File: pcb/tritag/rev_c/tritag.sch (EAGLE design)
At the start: 135 parts, among them J1 TC2030-JLINK-NL, J2 TC2030-JLINK-NL, J3 MICRO_USB_B_HIROSE_ZX62-B-5PA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, J5 BAT_HOLE, J7 CON_MICRO_SDDM3AT-SF-PEJM5, T1 HHM1595A1, U1 NRF52840, U12 SIP32510, U2 MCP73831, U3 FT232RQ, U4 MAX8887EZK33+T, U5 STM32F091CC, U6 SKY13317, U7 LXDC2HN18A, U8 DW1000, U9 LIS2DW12, X1 32MHz, X2 38.4M, X3 16M, X4 32.768kHz

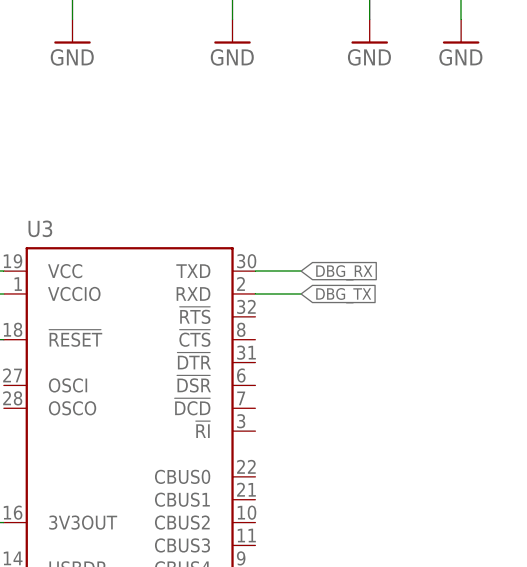
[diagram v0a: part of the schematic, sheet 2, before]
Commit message: added clearance for screws, decoupled FT232 to reduce power draw, added power planes
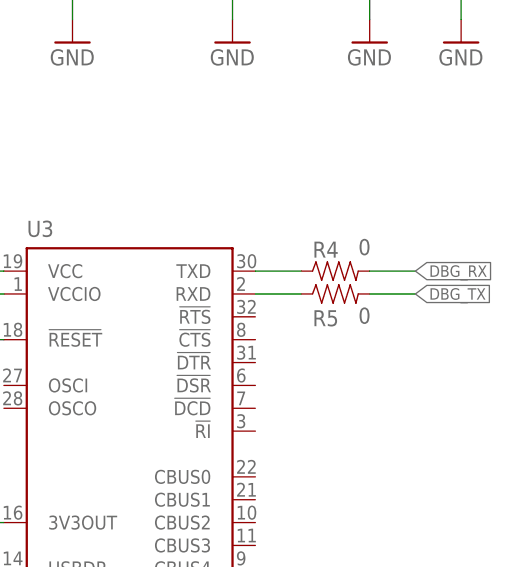
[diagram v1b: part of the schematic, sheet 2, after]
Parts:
- added R4, R5: 0, passives:RESISTOR0402_RES
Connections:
- new net N$33: R4.1, U3.TXD
- new net N$34: R5.1, U3.RXD
- net DBG_RX: now also R4.2; no longer U3.TXD
- net DBG_TX: now also R5.2; no longer U3.RXD
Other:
- note added: "Mount 0-Ohm resistors only if you intend to use the FTDI; this prevents unintentional power draws"
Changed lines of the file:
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@@
 <part name="TP12" library="headers" deviceset="TEST-POINT" device=""/>
 <part name="TP15" library="testpad" library_urn="urn:adsk.eagle:library:385" deviceset="TP" device="TP06SQ" package3d_urn="urn:adsk.eagle:package:27952/1"/>
+<part name="R4" library="passives" deviceset="RESISTOR" device="0402_RES" value="0"/>
+<part name="R5" library="passives" deviceset="RESISTOR" device="0402_RES" value="0"/>
 </parts>
 <sheets>
@@
 <wire x1="147.32" y1="55.88" x2="147.32" y2="53.34" width="0.1524" layer="98" style="longdash"/>
 <wire x1="147.32" y1="53.34" x2="147.32" y2="20.32" width="0.1524" layer="98" style="longdash"/>
-<text x="157.48" y="30.48" size="5.08" layer="98">USB-Serial</text>
+<text x="152.4" y="30.48" size="5.08" layer="98">USB-Serial</text>
 <text x="3.556" y="49.784" size="3.81" layer="98">SD Card Adapter</text>
 <wire x1="0" y1="55.88" x2="93.98" y2="55.88" width="0.1524" layer="98" style="longdash"/>
@@
 <wire x1="93.98" y1="55.88" x2="147.32" y2="55.88" width="0.1524" layer="98" style="longdash"/>
 <wire x1="93.98" y1="116.84" x2="93.98" y2="55.88" width="0.1524" layer="98" style="longdash"/>
+<text x="203.2" y="30.48" size="1.778" layer="98">Mount 0-Ohm resistors only
+if you intend to use the FTDI;
+this prevents unintentional
+power draws</text>
 </plain>
 <instances>
@@
 <instance part="A2" gate="G$1" x="119.38" y="88.9"/>
 <instance part="A1" gate="G$1" x="109.22" y="91.44"/>
+<instance part="R4" gate="G$1" x="231.14" y="101.6" smashed="yes">
+<attribute name="NAME" x="227.33" y="103.0986" size="1.778" layer="95"/>
+<attribute name="VALUE" x="232.41" y="103.378" size="1.778" layer="96"/>
+</instance>
+<instance part="R5" gate="G$1" x="231.14" y="99.06" smashed="yes">
+<attribute name="NAME" x="227.33" y="95.4786" size="1.778" layer="95"/>
+<attribute name="VALUE" x="232.41" y="95.758" size="1.778" layer="96"/>
+</instance>
 </instances>
 <busses>
@@
 <wire x1="58.42" y1="152.4" x2="63.5" y2="152.4" width="0.1524" layer="91"/>
 <label x="63.5" y="152.4" size="1.016" layer="95" xref="yes"/>
-</segment>
-</net>
-<net name="DBG_RX" class="0">
-<segment>
-<label x="226.06" y="101.6" size="1.27" layer="95" xref="yes"/>
-<pinref part="U3" gate="1" pin="TXD"/>
-<wire x1="220.98" y1="101.6" x2="226.06" y2="101.6" width="0.1524" layer="91"/>
 </segment>
 </net>
@@
 </segment>
 </net>
-<net name="DBG_TX" class="0">
-<segment>
-<pinref part="U3" gate="1" pin="RXD"/>
-<wire x1="220.98" y1="99.06" x2="226.06" y2="99.06" width="0.1524" layer="91"/>
-<label x="226.06" y="99.06" size="1.27" layer="95" xref="yes"/>
-</segment>
-</net>
 <net name="!FT_RST" class="0">
 <segment>
@@
 </segment>
 </net>
+<net name="N$33" class="0">
+<segment>
+<pinref part="U3" gate="1" pin="TXD"/>
+<pinref part="R4" gate="G$1" pin="1"/>
+<wire x1="220.98" y1="101.6" x2="226.06" y2="101.6" width="0.1524" layer="91"/>
+</segment>
+</net>
+<net name="N$34" class="0">
+<segment>
+<pinref part="U3" gate="1" pin="RXD"/>
+<pinref part="R5" gate="G$1" pin="1"/>
+<wire x1="220.98" y1="99.06" x2="226.06" y2="99.06" width="0.1524" layer="91"/>
+</segment>
+</net>
+<net name="DBG_RX" class="0">
+<segment>
+<pinref part="R4" gate="G$1" pin="2"/>
+<wire x1="233.68" y1="101.6" x2="238.76" y2="101.6" width="0.1524" layer="91"/>
+<label x="238.76" y="101.6" size="1.27" layer="95" xref="yes"/>
+</segment>
+</net>
+<net name="DBG_TX" class="0">
+<segment>
+<pinref part="R5" gate="G$1" pin="2"/>
+<wire x1="233.68" y1="99.06" x2="238.76" y2="99.06" width="0.1524" layer="91"/>
+<label x="238.76" y="99.06" size="1.27" layer="95" xref="yes"/>
+</segment>
+</net>

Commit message: renumbered parts, added decaps for power supply
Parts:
- removed C75: 0.1uF, passives:CAPACITOR0402_CAP
- removed C77: 4.7uF, passives:CAPACITOR0402_CAP
- removed C78: 1pF, passives:CAPACITOR0402_CAP
- removed C79: 1uF, passives:CAPACITOR0402_CAP
- removed C80: 47nF, passives:CAPACITOR0402_CAP
- removed C81, C82: 12pF, passives:CAPACITOR0402_CAP
- removed D5: SML-LX0404SIUPGUSB, leds:SML-LX0404SIUPGUSB
- removed J7: CON_MICRO_SDDM3AT-SF-PEJM5, connector:CON_MICRO_SDDM3AT-SF-PEJM5
- removed R23: 10k, passives:RESISTOR0402_RES
- removed R27, R28, R29: 470, passives:RESISTOR0402_RES
- removed U12: SIP32510, chips:SIP32510
- added C61, C62, C63, C64, C65, C66, C67, C68: 4.7uF, passives:CAPACITOR0402_CAP
- added C70: 10uF, passives:CAPACITOR0603_CAP
- added D3: SML-LX0404SIUPGUSB, leds:SML-LX0404SIUPGUSB
- added J4: TC2030-JLINK-NL, connector:TC2030-JLINK-NL
- added R15: 11k 1%, passives:RESISTOR0402_RES
- added R16: 11k, passives:RESISTOR0402_RES
- added R17: 16k, passives:RESISTOR0402_RES
- added R18: 100k, passives:RESISTOR0402_RES
- added U10: STM32F091CC, chips:STM32F091CC
- C1: value 4.7uF -> 1pF; DIGIKEY 445-5947-1-ND -> 490-6269-1-ND; MPN C1005X5R0J475K050BC -> GRM1555C1HR80BA01D
- C10, C11: value 4.7uF -> 12pF; DIGIKEY (none) -> 490-6197-1-ND; MPN (none) -> GRM1555C1H120GA01D
- C12: DIGIKEY 490-6197-1-ND -> (none); MPN GRM1555C1H120GA01D -> (none)
- C13: value 1uF -> 12pF
- C14: value 1pF -> 12pF; DIGIKEY 490-6269-1-ND -> (none); MPN GRM1555C1HR80BA01D -> (none)
- C15: value 10nF -> 12pF
- C16: value 12pF -> 18pF; device passives:CAPACITOR0201_CAP -> passives:CAPACITOR0402_CAP
- C17: value 12pF -> 27pF; device passives:CAPACITOR0201_CAP -> passives:CAPACITOR0402_CAP
- C18: value 4.7uF -> 100pF; DIGIKEY (none) -> 490-5922-1-ND; MPN (none) -> GRM1555C1H101JA01D
- C19: value 10uF -> 330pF; device passives:CAPACITOR0603_CAP -> passives:CAPACITOR0402_CAP
- C2: value 0.1uF -> 1pF; DIGIKEY 490-6328-1-ND -> 490-6264-1-ND; MPN GRM155R71C104KA88J -> GRM1555C1HR50WA01D
- C20: value 0.1uF -> 330pF
- C21: value 4.7uF -> 820pF; DIGIKEY (none) -> 445-1264-1-ND; MPN (none) -> C1005X7R1C473K050BC
- C22: value 0.1uF -> 820pF
- C23, C24, C25: value 0.1uF -> 10nF
- C26: value 0.1uF -> 47nF; DIGIKEY (none) -> 445-1264-1-ND; MPN (none) -> C1005X7R1C473K050BC
- C28, C29, C30: DIGIKEY (none) -> 490-6328-1-ND; MPN (none) -> GRM155R71C104KA88J
- C3: value 0.1uF -> 1.2pF; DIGIKEY 490-6328-1-ND -> (none); MPN GRM155R71C104KA88J -> (none)
- C31, C32: value 10pF -> 0.1uF; DIGIKEY (none) -> 490-6328-1-ND; MPN (none) -> GRM155R71C104KA88J
- C33: value 330pF -> 0.1uF; DIGIKEY (none) -> 490-6328-1-ND; MPN (none) -> GRM155R71C104KA88J
- C34: value 330pF -> 0.1uF
- C35: value 0.01uF -> 0.1uF
- C4, C5: value 0.1uF -> 10pF; DIGIKEY 490-6328-1-ND -> (none); MPN GRM155R71C104KA88J -> (none)
- C41: value 820pF -> 0.1uF
- C42: value 27pF -> 0.1uF
- C43: value 1.2pF -> 0.1uF
- C44: value 18pF -> 0.1uF
- C45, C46, C47, C48: value 12pF -> 0.1uF
- C49, C50, C51: value 100nF -> 0.1uF
- C52, C53: value 4.7uF -> 0.1uF
- C54: value 100nF -> 1uF
- C55: DIGIKEY (none) -> 490-7195-1-ND; MPN (none) -> GRM155R70G105KA12D
- C56: value 10nF -> 1uF; DIGIKEY (none) -> 490-7195-1-ND; MPN (none) -> GRM155R70G105KA12D
- C57: value 0.1uF -> 1uF
- C59: value 0.1uF -> 4.7uF; DIGIKEY 490-6328-1-ND -> (none); MPN GRM155R71C104KA88J -> (none)
- C6: value 1uF -> 12pF; device passives:CAPACITOR0402_CAP -> passives:CAPACITOR0201_CAP; DIGIKEY 490-7195-1-ND -> (none); MPN GRM155R70G105KA12D -> (none)
- C60: value 820pF -> 4.7uF; DESCRIPTION (none) -> CAP CER 4.7UF 6.3V X5R 0402; DIGIKEY 445-1264-1-ND -> 445-5947-1-ND; MANUFACTURER (none) -> TDK; MPN C1005X7R1C473K050BC -> C1005X5R0J475K050BC
- C7: value 100pF -> 12pF; device passives:CAPACITOR0402_CAP -> passives:CAPACITOR0201_CAP; DIGIKEY 490-5922-1-ND -> (none); MPN GRM1555C1H101JA01D -> (none)
- C9: value 0.1uF -> 12pF; DIGIKEY (none) -> 490-6197-1-ND; MPN (none) -> GRM1555C1H120GA01D
- J1: value TC2030-JLINK-NL -> BAT_HOLE; device connector:TC2030-JLINK-NL -> connector:BAT_HOLE
- J2: value TC2030-JLINK-NL -> CON_MICRO_SDDM3AT-SF-PEJM5; device connector:TC2030-JLINK-NL -> connector:CON_MICRO_SDDM3AT-SF-PEJM5
- J5: value BAT_HOLE -> TC2030-JLINK-NL; device connector:BAT_HOLE -> connector:TC2030-JLINK-NL
- R1: value 270 -> 0
- R10: value 11k -> 1k
- R11: value 1k -> 2k 1%
- R12, R13: value 1k -> 10k
- R14: value 100k -> 10k
- R2: value 1k -> 0
- R21: value 10k -> 2.2M
- R22: value 10k -> 10M
- R3: value 2k 1% -> 270
- R4, R5: value 0 -> 470
- R6: value 16k -> 470
- R7: value 2.2M -> 1k
- R8: value 10M -> 1k
- R9: value 11k 1% -> 1k
- U1: value NRF52840 -> DW1000; device chips:NRF52840 -> chips:DW1000
- U2: value MCP73831 -> FT232RQ; device chips:MCP73831 -> ftdichip:FT232RQ
- U3: value FT232RQ -> LIS2DW12; device ftdichip:FT232RQ -> chips:LIS2DW12
- U4: value MAX8887EZK33+T -> LXDC2HN18A; device chips:MAX8887EZK33+T -> regulators:LXDC2HN18A
- U5: value STM32F091CC -> MAX8887EZK33+T; device chips:STM32F091CC -> chips:MAX8887EZK33+T
- U6: value SKY13317 -> MCP73831; device switches:SKY13317 -> chips:MCP73831
- U7: value LXDC2HN18A -> NRF52840; device regulators:LXDC2HN18A -> chips:NRF52840
- U8: value DW1000 -> SIP32510; device chips:DW1000 -> chips:SIP32510
- U9: value LIS2DW12 -> SKY13317; device chips:LIS2DW12 -> switches:SKY13317
- X1: value 32MHz -> 32.768kHz; device crystals:7V-32.000MAHV-T -> crystals:ABS05-32.768KHZ-9-T
- X2: value 38.4M -> 16MHz; DESCRIPTION 38.4MHz ±10ppm Crystal 8.5pF 40 Ohms 4-SMD, No Lead -> 16MHz ±10ppm Crystal 8pF 80 Ohms 4-SMD, No Lead; DIGIKEY SER3631CT-ND -> SER3913CT-ND
- X3: value 16M -> 32MHz; device crystals:FA-20H -> crystals:7V-32.000MAHV-T; DESCRIPTION 16MHz ±10ppm Crystal 8pF 80 Ohms 4-SMD, No Lead -> (none); DIGIKEY SER3913CT-ND -> (none)
- X4: value 32.768kHz -> 38.4MHz; device crystals:ABS05-32.768KHZ-9-T -> crystals:FA-20H; DESCRIPTION (none) -> 38.4MHz ±10ppm Crystal 8.5pF 40 Ohms 4-SMD, No Lead; DIGIKEY (none) -> SER3631CT-ND
- renumbered C76 to C69
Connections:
- net !CHRG: now also R7.1; no longer R2.1
- net !DW_RST: now also U1.!RST, U10.PB0; no longer U5.PB0, U8.!RST
- net !DW_SPI_CS: now also U1.!SPICS, U10.PA4; no longer U5.PA4, U8.!SPICS
- net !FT_RST: now also U2.!RESET, U7.P1.08; no longer U1.P1.08, U3.!RESET
- net !NRF_CS_IMU: now also U3.CS, U7.P0.16; no longer U1.P0.16, U9.CS
- net !NRF_CS_SD: now also J2.DATA3-CD/CS_N, R13.1, U7.P0.18; no longer J7.DATA3-CD/CS_N, R22.1, U1.P0.18
- net !SD_DETECT: now also J2.A, R19.1, U7.P1.00; no longer J7.A, R20.1, U1.P1.00
- net !STM_RST: now also J5.!RESET, U10.!RST; no longer J2.!RESET, U5.!RST
- net +1V8: now also C34.1, C37.1, C63.1, C70.1, U1.VDDLDOA, U1.VDDLDOD, U4.VOUT; no longer C19.1, C20.1, C21.1, C24.1, U7.VOUT, U8.VDDLDOA, U8.VDDLDOD
- net +3V3: now also C19.1, C20.1, C24.1, C25.1, C29.1, C30.1, C4.1, C44.1, C45.1, C46.1, C47.1, C48.1, C57.1, C59.1, C61.1, C62.2, C64.1, C65.1, C66.1, D3.VDD, J4.VCC, J5.VCC, U1.VDDAON, U1.VDDBAT, U1.VDDIOA, U1.VDDLNA, U1.VDDPA1, U1.VDDPA2, U10.VBAT, U10.VDD/24, U10.VDD/48, U10.VDDA, U10.VDDIO2, U3.VCC, U3.VDD_IO, U4.VIN, U5.OUT, U7.VDD, U7.VDDH, U8.VSUPP; no longer C1.1, C11.1, C18.2, C2.1, C3.1, C32.1, C34.1, C35.1, C36.1, C37.1, C38.1, C39.1, C40.1, C53.1, C54.1, C56.1, C58.1, C6.1, C75.1, D5.VDD, J1.VCC, J2.VCC, U1.VDD, U1.VDDH, U12.VSUPP, U4.OUT, U5.VBAT, U5.VDD/24, U5.VDD/48, U5.VDDA, U5.VDDIO2, U7.VIN, U8.VDDAON, U8.VDDBAT, U8.VDDIOA, U8.VDDLNA, U8.VDDPA1, U8.VDDPA2, U9.VCC, U9.VDD_IO
- net ANT_SEL1: now also U10.PB14, U9.V1; no longer U5.PB14, U6.V1
- net ANT_SEL2: now also U10.PB13, U9.V2; no longer U5.PB13, U6.V2
- net ANT_SEL3: now also U10.PB12, U9.V3; no longer U5.PB12, U6.V3
- net BATIN: now also C27.2, R21.2, R22.1; no longer C9.2, R7.2, R8.1
- net D+: now also U2.USBDP; no longer U3.USBDP
- net D-: now also U2.USBDM; no longer U3.USBDM
- net DBG_RX: now also R1.2, U7.P0.07; no longer R4.2, U1.P0.07
- net DBG_TX: now also R2.2, U7.P0.11; no longer R5.2, U1.P0.11
- net DW_IRQ: now also R20.2, U1.IRQ/GPIO8, U10.PB2; no longer R14.2, U5.PB2, U8.IRQ/GPIO8
- net DW_SPI_CLK: now also U1.SPICLK, U10.PA5; no longer U5.PA5, U8.SPICLK
- net DW_SPI_MISO: now also U1.SPIMISO, U10.PA6; no longer U5.PA6, U8.SPIMISO
- net DW_SPI_MOSI: now also U1.SPIMOSI, U10.PA7; no longer U5.PA7, U8.SPIMOSI
- net DW_SYNC: now also U1.SYNC/GPIO7; no longer U8.SYNC/GPIO7
- net DW_WAKEUP: now also U1.WAKEUP, U10.PB1; no longer U5.PB1, U8.WAKEUP
- net EXT_I2C_SCL: now also U10.PA9, U7.P1.09; no longer U1.P1.09, U5.PA9
- net EXT_I2C_SDA: now also U10.PA10, U7.P0.12; no longer U1.P0.12, U5.PA10
- net GND: now also C10.1, C11.1, C12.2, C16.2, C17.2, C18.2, C27.1, C61.2, C62.1, C63.2, C64.2, C65.2, C66.2, C67.2, C68.2, C70.2, J1.-, J2.B, J4.GND, J5.GND, R11.1, R15.1, R16.2, R18.2, R20.1, R21.1, U1.FORCEON, U1.GND, U1.TESTMODE, U1.VSSIO/32, U1.VSSIO/43, U10.GND, U10.VSS/23, U10.VSS/35, U10.VSS/47, U10.VSSA, U2.GND@1, U2.GND@2, U2.GND@A, U2.TEST, U6.VSS, U7.VBUS, U7.VSS, U7.VSS_PA, X4.GND; no longer C10.2, C11.2, C12.1, C18.1, C27.2, C6.2, C7.2, C75.2, C77.2, C78.2, C79.2, C80.2, C81.1, C82.1, J1.GND, J5.-, J7.B, J7.GND, R10.2, R14.1, R19.2, R3.1, R7.1, R9.1, U1.VBUS, U1.VSS, U1.VSS_PA, U12.GND, U2.VSS, U3.GND@1, U3.GND@2, U3.GND@A, U3.TEST, U5.VSS/23, U5.VSS/35, U5.VSS/47, U5.VSSA, U7.GND, U8.FORCEON, U8.TESTMODE, U8.VSSIO/32, U8.VSSIO/43, X1.GND
- net GPIO0: now also U10.PB6; no longer U5.PB6
- net GPIO1: now also U10.PB7; no longer U5.PB7
- net GPIO2: now also U10.PA8; no longer U5.PA8
- net GPIO3: now also U10.PB15; no longer U5.PB15
- net LED_BLUE: now also R10.2, U10.PB4; no longer R13.2, U5.PB4
- net LED_GREEN: now also R9.2, U10.PB5; no longer R12.2, U5.PB5
- net LED_NRF_BLUE: now also R6.2, U7.P0.04/AIN2; no longer R29.2, U1.P0.04/AIN2
- net LED_NRF_GREEN: now also R5.2, U7.P0.06; no longer R28.2, U1.P0.06
- net LED_NRF_RED: now also R4.2, U7.P0.05/AIN3; no longer R27.2, U1.P0.05/AIN3
- net LED_RED: now also R8.2, U10.PB3; no longer R11.2, U5.PB3
- net N$1: now also C28.1, U2.3V3OUT, U2.VCCIO; no longer C59.1, U3.3V3OUT, U3.VCCIO
- net N$10: now also C18.1, U7.DEC3; no longer C7.1, U1.DEC3
- net N$11: now also C23.1, U5.BP; no longer C15.1, U4.BP
- net N$12: now also C17.1, R17.2; no longer C42.1, R6.2
- net N$13: now also R11.2, U6.PROG; no longer R3.2, U2.PROG
- net N$14: now also C16.1, R3.1, U1.VCOTUNE; no longer C44.1, R1.1, U8.VCOTUNE
- net N$15: now also C1.1, U7.ANT; no longer C14.1, U1.ANT
- net N$16: now also C3.1, R17.1, U1.CLKTUNE; no longer C43.1, R6.1, U8.CLKTUNE
- net N$17: now also C2.1; no longer C78.1
- net N$18: now also U7.XC1, X3.2; no longer U1.XC1, X1.2
- net N$19: now also C9.2, U7.XC2, X3.1; no longer C12.2, U1.XC2, X1.1
- net N$2: now also C21.1, U7.DEC5; no longer C60.1, U1.DEC5
- net N$20: now also U7.DCC; no longer U1.DCC
- net N$21: now also R15.2, U1.VREF; no longer R9.2, U8.VREF
- net N$22: now also R16.1, U10.PF11-BOOT0; no longer R10.1, U5.PF11-BOOT0
- net N$23: now also D3.G, R9.1; no longer D2.G, R12.1
- net N$24: now also D3.B, R10.1; no longer D2.B, R13.1
- net N$25: now also D3.R, R8.1; no longer D2.R, R11.1
- net N$26: now also U1.GPIO2; no longer U8.GPIO2
- net N$27: now also U1.GPIO3; no longer U8.GPIO3
- net N$3: now also U9.RFC; no longer U6.RFC
- net N$33: now also R1.1, U2.TXD; no longer R4.1, U3.TXD
- net N$34: now also R2.1, U2.RXD; no longer R5.1, U3.RXD
- net N$4: now also C6.2; no longer C16.2
- net N$5: now also U6.STAT; no longer U2.STAT
- net N$55: now also C60.1, J2.VCC, R12.2, R13.2, R14.2, R19.2, U8.VLOAD; no longer C77.1, J7.VCC, R20.2, R21.2, R22.2, R23.2, U12.VLOAD
- net N$59: now also D2.R, R4.1; no longer D5.R, R27.1
- net N$6: now also C32.1, U7.DEC1; no longer C4.1, U1.DEC1
- net N$60: now also D2.G, R5.1; no longer D5.G, R28.1
- net N$61: now also D2.B, R6.1; no longer D5.B, R29.1
- net N$7: now also C7.2; no longer C17.2
- net N$8: now also C22.1, R3.2; no longer C41.1, R1.2
- net N$9: now also C26.1, C56.1, U7.DEC4, U7.DEC6; no longer C79.1, C80.1, U1.DEC4, U1.DEC6
- net NRF_GPIO_0: now also U7.P0.27; no longer U1.P0.27
- net NRF_GPIO_1: now also U7.P0.26; no longer U1.P0.26
- net NRF_IMU_INT1: now also U3.INT1, U7.P0.22; no longer U1.P0.22, U9.INT1
- net NRF_IMU_INT2: now also U3.INT2, U7.P0.24; no longer U1.P0.24, U9.INT2
- net NRF_MISO: now also J2.DATA0/MISO, R14.1, U3.MISO/SA0, U7.P0.15; no longer J7.DATA0/MISO, R23.1, U1.P0.15, U9.MISO/SA0
- net NRF_MOSI: now also J2.CMD/MOSI, R12.1, U3.MOSI/SDA, U7.P0.13; no longer J7.CMD/MOSI, R21.1, U1.P0.13, U9.MOSI/SDA
- net NRF_SCK: now also J2.CLK, U3.SCL/SPC, U7.P0.17; no longer J7.CLK, U1.P0.17, U9.SCL/SPC
- net NRF_SWDCLK: now also J4.SWDCLK, U7.SWDCLK; no longer J1.SWDCLK, U1.SWDCLK
- net NRF_SWDIO: now also J4.SWDIO, U7.SWDIO; no longer J1.SWDIO, U1.SWDIO
- net OSC_IN: now also C14.1, U10.PF0-OSC_IN, X2.1; no longer C47.1, U5.PF0-OSC_IN, X3.1
- net OSC_OUT: now also C15.1, U10.PF1-OSC_OUT, X2.2; no longer C48.1, U5.PF1-OSC_OUT, X3.2
- net REG_EN: now also U1.EXTON, U4.EN; no longer U7.EN, U8.EXTON
- net RF1: now also U9.RF1; no longer U6.RF1
- net RF2: now also U9.RF2; no longer U6.RF2
- net RF3: now also U9.RF3; no longer U6.RF3
- net RF_N: now also C6.1, U1.RF_N; no longer C16.1, U8.RF_N
- net RF_P: now also C7.1, U1.RF_P; no longer C17.1, U8.RF_P
- net SD_EN: now also R18.1, U7.P0.14, U8.EN; no longer R19.1, U1.P0.14, U12.EN
- net STM_INTERRUPT: now also U10.PA2, U7.P0.08; no longer U1.P0.08, U5.PA2
- net STM_SWCLK: now also J5.SWDCLK, U10.PA14; no longer J2.SWDCLK, U5.PA14
- net STM_SWDIO: now also J5.SWDIO, U10.PA13; no longer J2.SWDIO, U5.PA13
- net VBAT: now also C58.1, C68.1, J1.+, R22.2, U5.!SHDN, U5.IN, U6.VBAT/3, U6.VBAT/4; no longer C10.1, J5.+, R8.2, U2.VBAT/3, U2.VBAT/4, U4.!SHDN, U4.IN
- net VDDCLK: now also C39.1, U1.VDDCLK; no longer C26.1, U8.VDDCLK
- net VDDDIG: now also C35.1, C36.1, U1.VDDDIG, U1.VDDREG; no longer C22.1, C23.1, U8.VDDDIG, U8.VDDREG
- net VDDIF: now also C42.1, U1.VDDIF; no longer C29.1, U8.VDDIF
- net VDDIO: now also C41.1, C53.1, U1.VDDIO/31, U1.VDDIO/42; no longer C28.1, C57.1, U8.VDDIO/31, U8.VDDIO/42
- net VDDMS: now also C38.1, U1.VDDMS; no longer C25.1, U8.VDDMS
- net VDDSYN: now also C40.1, U1.VDDSYN; no longer C27.1, U8.VDDSYN
- net VDDVCO: now also C43.1, U1.VDDVCO; no longer C30.1, U8.VDDVCO
- net VUSB: now also C54.1, C67.1, R7.2, U2.VCC, U6.VDD/1, U6.VDD/2; no longer C13.1, R2.2, U2.VDD/1, U2.VDD/2, U3.VCC
- net XL3: now also C11.2, U7.P0.00/XL1, X1.1; no longer C82.2, U1.P0.00/XL1, X4.1
- net XL4: now also C10.2, U7.P0.01/XL2, X1.2; no longer C81.2, U1.P0.01/XL2, X4.2
- net XTAL1: now also C13.1, U1.XTAL1, X4.2; no longer C46.1, U8.XTAL1, X2.2
- net XTAL2: now also C12.1, U1.XTAL2, X4.1; no longer C45.1, U8.XTAL2, X2.1

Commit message: added BOM files with up-to-date (ready to order) components
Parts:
- C1: DIGIKEY 490-6269-1-ND -> 490-3083-1-ND; MPN GRM1555C1HR80BA01D -> GJM1555C1H1R0CB01D
- C2: DIGIKEY 490-6264-1-ND -> 490-3083-1-ND; MPN GRM1555C1HR50WA01D -> GJM1555C1H1R0CB01D
- C21: DIGIKEY 445-1264-1-ND -> 1276-6989-1-ND; MPN C1005X7R1C473K050BC -> CL05C821JB5NFNC
- L1: DIGIKEY 535-10426-1-ND -> AISC-0402-3N9G-TCT-ND; MPN AISC-0402-3N3J-T -> AISC-0402-3N9G-T
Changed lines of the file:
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@@
 </part>
 <part name="C1" library="passives" deviceset="CAPACITOR" device="0402_CAP" value="1pF">
-<attribute name="DIGIKEY" value="490-6269-1-ND"/>
-<attribute name="MPN" value="GRM1555C1HR80BA01D "/>
+<attribute name="DIGIKEY" value="490-3083-1-ND"/>
+<attribute name="MPN" value="GJM1555C1H1R0CB01D "/>
 </part>
 <part name="C2" library="passives" deviceset="CAPACITOR" device="0402_CAP" value="1pF">
-<attribute name="DIGIKEY" value="490-6264-1-ND"/>
-<attribute name="MPN" value="GRM1555C1HR50WA01D "/>
+<attribute name="DIGIKEY" value="490-3083-1-ND"/>
+<attribute name="MPN" value="GJM1555C1H1R0CB01D"/>
 </part>
 <part name="L1" library="passives" deviceset="INDUCTOR" device="0402" value="3.9nH">
-<attribute name="DIGIKEY" value="535-10426-1-ND"/>
-<attribute name="MPN" value="AISC-0402-3N3J-T "/>
+<attribute name="DIGIKEY" value="AISC-0402-3N9G-TCT-ND
+"/>
+<attribute name="MPN" value="AISC-0402-3N9G-T
+"/>
 </part>
 <part name="X3" library="crystals" deviceset="7V" device="-32.000MAHV-T" value="32MHz"/>
@@
 <part name="A1" library="chips" deviceset="TAIYO-YUDEN-AH086M" device=""/>
 <part name="C21" library="passives" deviceset="CAPACITOR" device="0402_CAP" value="820pF">
-<attribute name="DIGIKEY" value="445-1264-1-ND"/>
-<attribute name="MPN" value="C1005X7R1C473K050BC "/>
+<attribute name="DIGIKEY" value="1276-6989-1-ND"/>
+<attribute name="MPN" value="CL05C821JB5NFNC"/>
 </part>
 <part name="TP13" library="headers" deviceset="TEST-POINT" device=""/>
